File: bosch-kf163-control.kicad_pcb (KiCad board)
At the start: 4 copper layers, 46 x 72 mm, 123 parts, among them J101 TGA, J102 PROG, J201 S353/CDP18U42P, Q101 DTC143ZE, Q102 DTC143ZE, Q103 DTC143ZE, Q104 DTC143ZE, Q201 DTC143ZE, Q202 DTC143ZE, Q203 DTC143ZE, Q204 DTC143ZE, Q205 DTC143ZE, Q206 DTC143ZE, Q207 DTC143ZE, Q208 DTC143ZE, Q209 DTC143ZE, Q210 DTC143ZE, Q211 DTC143ZE, Q212 DTC143ZE, Q213 DTC143ZE, Q214 DTC143ZE, Q215 DTC143ZE, Q216 DTC143ZE, U101 74HC165D, U102 AMS1117-3.3, U103 ESP32-WROOM-32U, U201 74HC595PW, U202 74HC165D, U203 74HC595PW, U301 RS8752XK, U302 RS8752XK

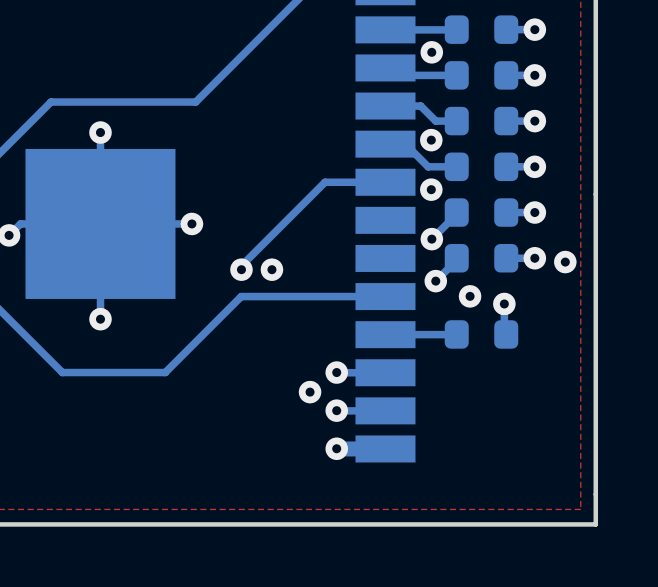
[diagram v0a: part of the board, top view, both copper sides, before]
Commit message: sheet comments, schematic variants, removed txd resistor
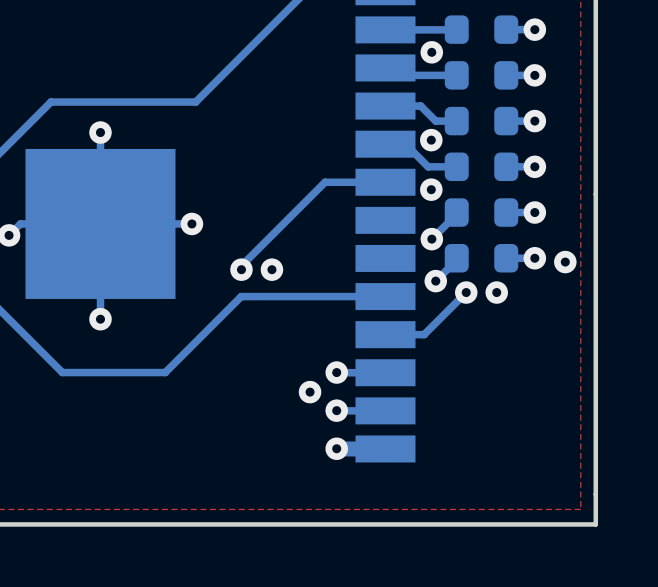
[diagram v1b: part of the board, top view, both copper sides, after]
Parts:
- removed R113: 1k, Resistor_SMD:R_0603_1608Metric
- C302, C306: value 10n -> 10n C0G
- C304, C308: value 1n -> 1n C0G
- R201, R202, R203, R204, R205, R206, R207: value 10k -> 4.7k
- R308, R309, R314, R315: value 4.7k -> TBD
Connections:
- U103 pad 35: Net-(R113-Pad1) -> TXD
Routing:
- net Net-(R113-Pad1): track 2.38 -> 0.00 mm
- net TXD: track 82.1 -> 83.4 mm

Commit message: silkscreen symbols and text, various schematic/pcb updates
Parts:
- added REF**: OSHW-Logo_11.4x12mm_SilkScreen, Symbol:OSHW-Logo_11.4x12mm_SilkScreen, F.Cu at (97.0, 71.9)
- added REF**: KiCad-Logo2_5mm_SilkScreen, Symbol:KiCad-Logo2_5mm_SilkScreen, F.Cu at (123.0, 127.0)
- added kibuzzard-61EB1225: G***, kibuzzard-61EB1225, F.Cu at (97.2, 87.6)
- added kibuzzard-61EB122B: G***, kibuzzard-61EB122B, F.Cu at (97.2, 90.2)
- added kibuzzard-61EB1233: G***, kibuzzard-61EB1233, F.Cu at (97.2, 82.6)
- added kibuzzard-61EB123A: G***, kibuzzard-61EB123A, F.Cu at (97.2, 85.1)
- added kibuzzard-61EB12C7: G***, kibuzzard-61EB12C7, F.Cu at (109.2, 111.6)
- added kibuzzard-61EB12DB: G***, kibuzzard-61EB12DB, F.Cu at (124.3, 111.9)
- added kibuzzard-61EB14A1: G***, kibuzzard-61EB14A1, F.Cu at (107.0, 78.0)
- added kibuzzard-61EB1504: G***, kibuzzard-61EB1504, F.Cu at (112.0, 78.0)
- D101, D102, D103, D201, D202, D203, D204, D205, D206, D207, D208, D209, D210, D211, D212, D213, D214: value SD103AW -> SD103AWS; footprint Diode_SMD:D_SOD-123 -> Diode_SMD:D_SOD-323
- J102: footprint Connector_PinHeader_2.54mm:PinHeader_1x04_P2.54mm_Horizontal -> Connector_PinHeader_2.54mm:PinHeader_1x04_P2.54mm_Vertical
- moved Q103 3.24 mm to (105.0, 116.1)
- moved D209 3.02 mm to (97.4, 80.3)
- moved D202 1.53 mm to (100.3, 85.3)
- moved D204 1.25 mm to (100.3, 69.1)
- moved D210 1.02 mm to (100.3, 83.4)
- moved D212 0.81 mm to (98.4, 69.1)
- moved D102 0.72 mm to (104.0, 121.4)
- moved D201 0.65 mm to (95.5, 80.3), turned to 90 degrees
- moved D205 0.52 mm to (96.5, 69.1)
- moved D203 0.52 mm to (100.3, 81.5)
- moved D206 0.51 mm to (94.2, 69.1)
- moved D103 0.40 mm to (101.1, 116.2)
- moved D101 0.38 mm to (101.1, 118.5)
- moved C201 0.15 mm to (91.4, 76.6)
- moved R204 0.13 mm to (91.7, 67.1)
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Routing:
- net Net-(D201-Pad1): track 31.7 -> 27.3 mm
- net PTT_OUT: track 9.73 -> 5.63 mm, vias 0 -> 2
- net /SQUELCH: track 28.5 -> 25.0 mm
- net LATCH: track 130.3 -> 127.0 mm
- net CLK: track 122.6 -> 119.5 mm
- net GND: track 90.7 -> 93.4 mm, vias 113 -> 124
- net Net-(D202-Pad2): track 36.8 -> 34.4 mm
- net Net-(D202-Pad1): track 62.5 -> 64.7 mm
- net Net-(D210-Pad1): track 62.6 -> 64.5 mm
- net Net-(D209-Pad1): track 22.8 -> 24.6 mm
- net Net-(D212-Pad2): track 11.2 -> 9.81 mm
- net Net-(D204-Pad2): track 29.7 -> 31.0 mm
- net Net-(D212-Pad1): track 99.3 -> 100.5 mm
- net PTT_SENSE: track 17.8 -> 16.7 mm
- net +3V3: track 268.4 -> 267.3 mm
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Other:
- board text added: "X: place only for DigX PLL D: place only for diode PLL U: place for external UART"
